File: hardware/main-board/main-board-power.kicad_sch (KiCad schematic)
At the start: 38 parts, among them J3 Power Board, J4 DMX512, U4 RT8258, U5 RT8258

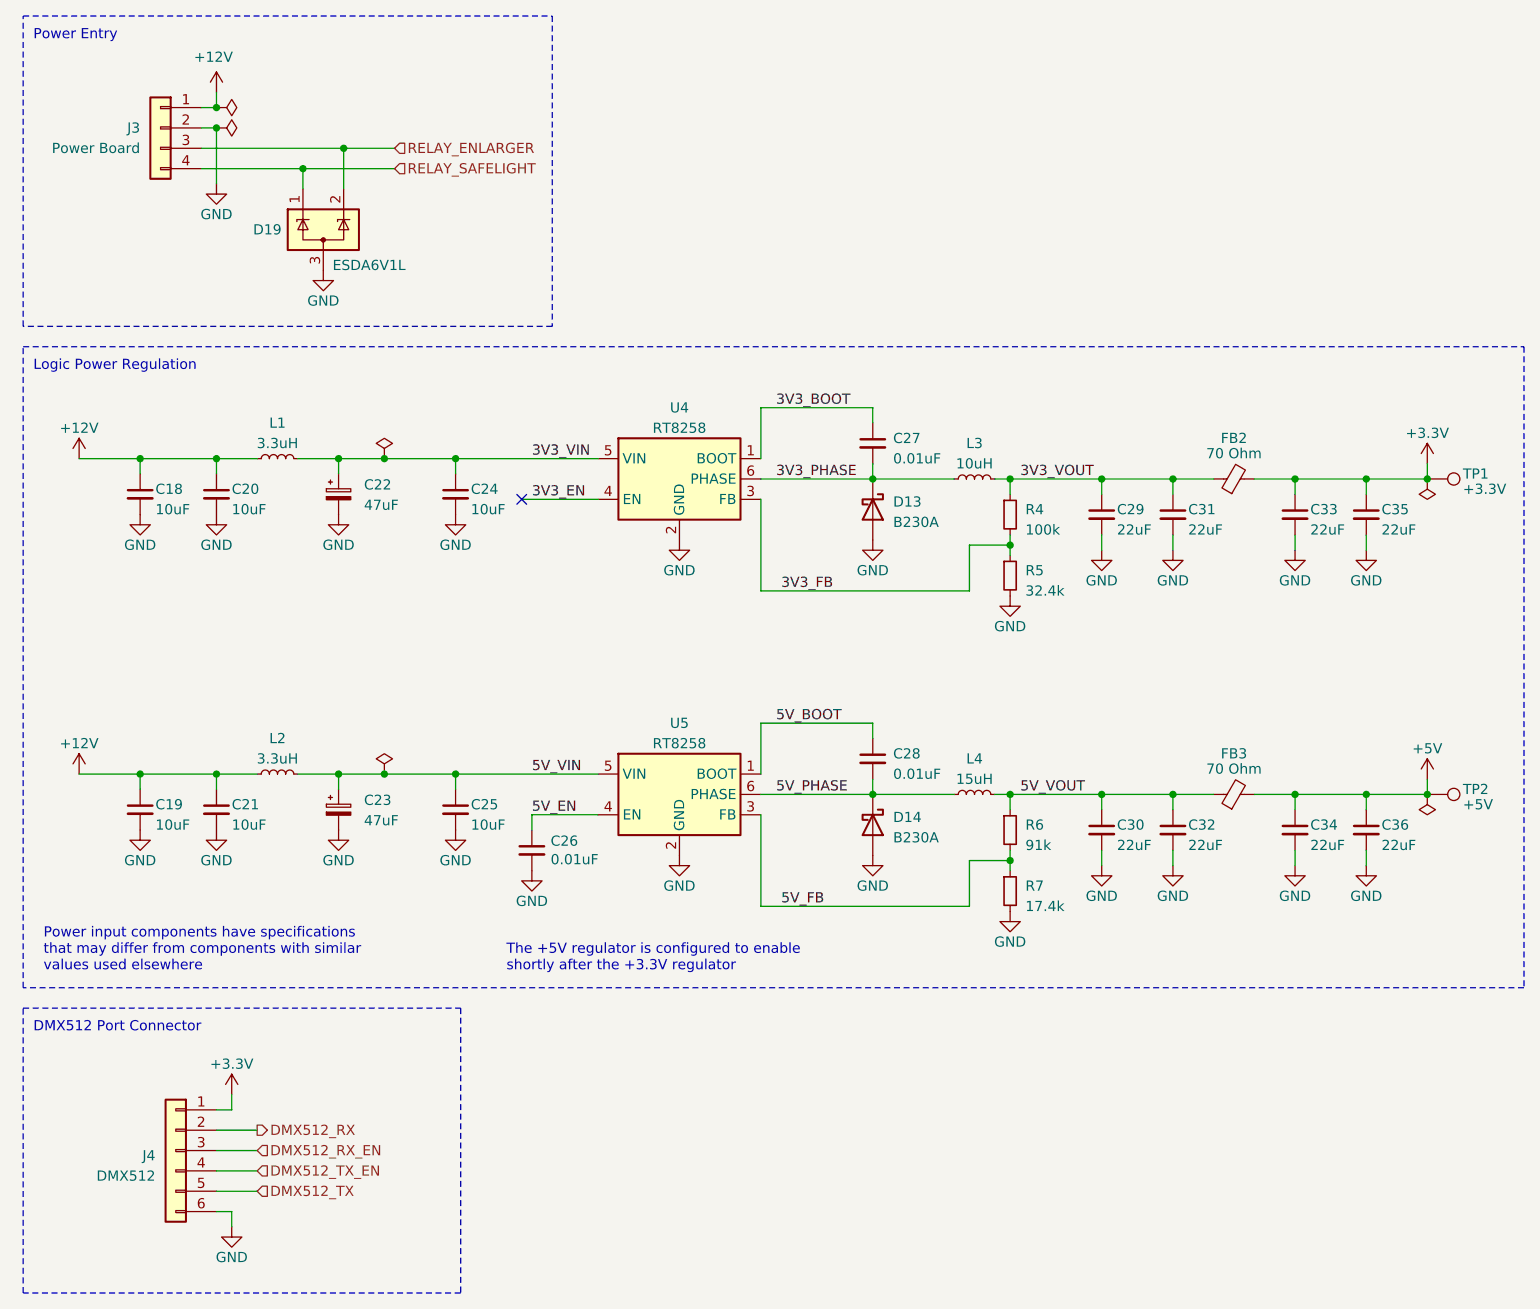
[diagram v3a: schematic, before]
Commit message: Initial replacement of main board power regulator
This is the first step towards updating the power input path for the
main board.  Right now it is mostly just a copy-paste of the TPS54294
circuit and layout from a test board, so there will be more tweaks.

Ref #67
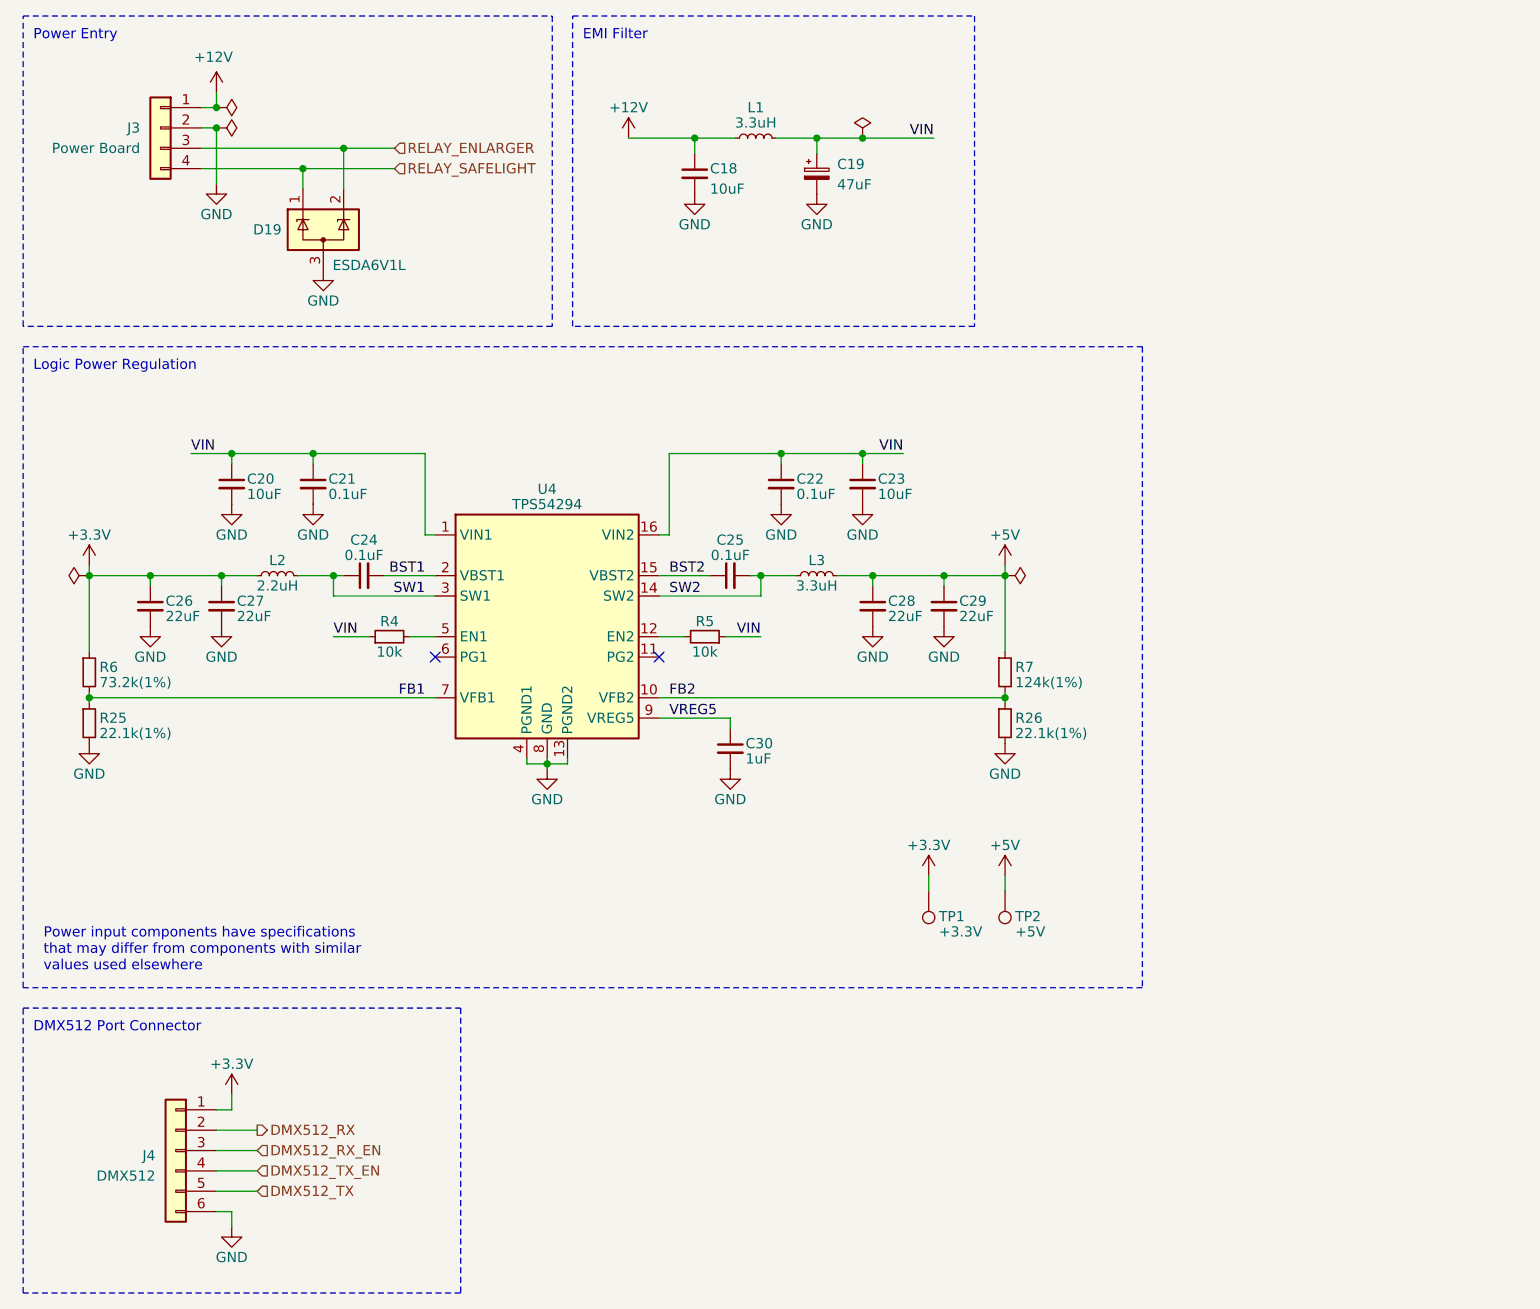
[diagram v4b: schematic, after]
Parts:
- removed C19: 10uF, Capacitor_SMD:C_1206_3216Metric, symbol Device:C_Small
- removed C22, C23: 47uF, Capacitor_SMD:CP_Elec_6.3x5.4, symbol Device:C_Polarized_Small
- removed C31, C32, C33, C34, C35, C36: 22uF, Capacitor_SMD:C_1206_3216Metric, symbol Device:C_Small
- removed D13, D14: B230A, Diode_SMD:D_SMA, symbol Diode:B230
- removed FB2, FB3: 70 Ohm, Inductor_SMD:L_0603_1608Metric, symbol Device:FerriteBead_Small
- removed L4: 15uH, Inductor_SMD:L_Taiyo-Yuden_NR-80xx, symbol Device:L_Small
- removed U4, U5: RT8258, Package_TO_SOT_SMD:TSOT-23-6, symbol Project:RT8258
- added C19: 47uF, Capacitor_SMD:CP_Elec_6.3x5.4, symbol Device:C_Polarized_Small
- added C22: 0.1uF, Capacitor_SMD:C_0603_1608Metric, symbol Device:C_Small
- added C23: 10uF, Capacitor_SMD:C_1206_3216Metric, symbol Device:C_Small
- added R25, R26: 22.1k(1%), Resistor_SMD:R_0603_1608Metric, symbol Device:R_Small
- added U4: TPS54294, lib_fp:HTSSOP-16-1EP_4.4x5mm_P0.65mm_EP3.4x5mm_Mask2.46x2.31mm_ThermalVias, symbol Project:TPS54294
- C21, C24, C25: value 10uF -> 0.1uF; footprint Capacitor_SMD:C_1206_3216Metric -> Capacitor_SMD:C_0603_1608Metric; Manufacturer PN CL31A106KAHNNNE -> CL10B104KB8NNNC; Supplier PN 1276-1075-1-ND -> 1276-1000-1-ND
- C26, C27, C28: value 0.01uF -> 22uF; footprint Capacitor_SMD:C_0603_1608Metric -> Capacitor_SMD:C_0805_2012Metric; Manufacturer PN CL10B103KB8NNNC -> CL21A226MOCLRNC; Supplier PN 1276-1009-1-ND -> 1276-6780-1-ND
- C29: footprint Capacitor_SMD:C_1206_3216Metric -> Capacitor_SMD:C_0805_2012Metric; Manufacturer PN CL31A226KAHNNNE -> CL21A226MOCLRNC; Supplier PN 1276-3047-1-ND -> 1276-6780-1-ND
- C30: value 22uF -> 1uF; footprint Capacitor_SMD:C_1206_3216Metric -> Capacitor_SMD:C_0603_1608Metric; Manufacturer PN CL31A226KAHNNNE -> CL10B105KA8NNNC; Supplier PN 1276-3047-1-ND -> 1276-1184-1-ND
- L1: footprint Inductor_SMD:L_Taiyo-Yuden_NR-50xx -> Inductor_SMD:L_TDK_VLS6045EX_VLS6045AF; Manufacturer Taiyo Yuden -> TDK Corporation; Manufacturer PN NRS5030T3R3MMGJ -> VLS6045EX-3R3N; Supplier PN 587-3459-1-ND -> 445-173052-1-ND
- L2: value 3.3uH -> 2.2uH; footprint Inductor_SMD:L_Taiyo-Yuden_NR-50xx -> Inductor_SMD:L_TDK_VLS6045EX_VLS6045AF; Manufacturer Taiyo Yuden -> TDK Corporation; Manufacturer PN NRS5030T3R3MMGJ -> VLS6045EX-2R2N; Supplier PN 587-3459-1-ND -> 445-173049-1-ND
- L3: value 10uH -> 3.3uH; footprint Inductor_SMD:L_Taiyo-Yuden_NR-80xx -> Inductor_SMD:L_TDK_VLS6045EX_VLS6045AF; Manufacturer Taiyo Yuden -> TDK Corporation; Manufacturer PN NRS8040T100MJGJ -> VLS6045EX-3R3N; Supplier PN 587-2972-1-ND -> 445-173052-1-ND
- R4: value 100k -> 10k; Manufacturer Panasonic Electronic Components -> Vishay Dale; Manufacturer PN ERJ-3EKF1003V -> CRCW060310K0JNEA; Supplier PN P100KHCT-ND -> 541-10KGCT-ND
- R5: value 32.4k -> 10k; Manufacturer Panasonic Electronic Components -> Vishay Dale; Manufacturer PN ERJ-3EKF3242V -> CRCW060310K0JNEA; Supplier PN P32.4KHCT-ND -> 541-10KGCT-ND
- R6: value 91k -> 73.2k(1%); Manufacturer Panasonic Electronic Components -> YAGEO; Manufacturer PN ERJ-3EKF9102V -> RC0603FR-0773K2L; Supplier PN P91.0KHCT-ND -> 311-73.2KHRCT-ND
- R7: value 17.4k -> 124k(1%); Manufacturer Panasonic Electronic Components -> YAGEO; Manufacturer PN ERJ-3EKF1742V -> RC0603FR-07124KL; Supplier PN P17.4KHCT-ND -> 311-124KHRCT-ND
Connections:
- net 3V3_BOOT is gone; now on net +3.3V: C27.1
- net 5V_BOOT is gone; now on net +5V: C28.1
- net 5V_EN is gone; now on net +3.3V: C26.1
- net 5V_PHASE is gone; now on net GND: C28.2
- net +12V: no longer C20.1, C21.1, L2.1
- net +3.3V: now also L2.1, R6.1
- net +5V: now also C29.1, L3.2, R7.1
- net GND: now also C27.2, C19.2, C22.2, C23.2, R25.2, R26.2, U4.13 (PGND2), U4.17 (GND), U4.4 (PGND1), U4.8 (GND); no longer C24.2, C25.2, R5.2, R7.2
- net 3V3_FB: no longer names the net of R4.2
- net 3V3_FB: now also U4.5 (EN1); no longer R5.1
- net 3V3_PHASE renamed SW2
- net SW2: now also C25.2, U4.14 (SW2); no longer C27.2
- net 3V3_VIN renamed SW1
- net SW1: now also L2.2, U4.3 (SW1); no longer L1.2
- removed net 3V3_VOUT: C29.1, L3.2, R4.1
- net 5V_FB renamed FB1
- net FB1: now also R25.1, U4.7 (VFB1); no longer R7.1
- net 5V_VIN renamed BST2
- net BST2: now also U4.15 (VBST2); no longer L2.2
- net 5V_VOUT renamed VREG5
- net VREG5: now also U4.9 (VREG5); no longer R6.1
- new net: R5.2, U4.12 (EN2)
- new net BST1: C24.2, U4.2 (VBST1)
- new net FB2: R26.1, R7.2, U4.10 (VFB2)
- new net VIN: C19.1, C20.1, C21.1, C22.1, C23.1, L1.2, R4.1, R5.1, U4.1 (VIN1), U4.16 (VIN2)
- no-connect marks 1 -> 2
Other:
- note added: "EMI Filter"
- note removed: "The +5V regulator is configured to enable shortly after the +3.3V regulator"
- moved on the sheet: TP1, TP2

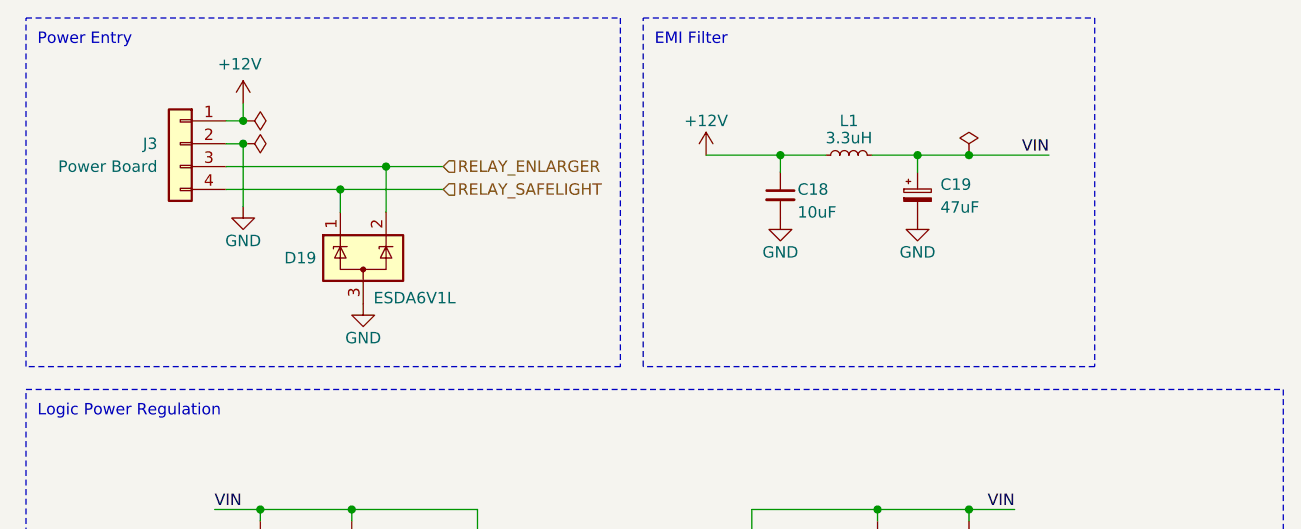
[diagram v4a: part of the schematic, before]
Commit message: Add power input filter components
For now, this is just the TVS diode and ferrite beads mentioned in the
reference app note.  For the capacitors, just using the ones from the
EMI filter as it is the next stage.

Also increased the value of the electrolytic capacitor in the EMI
filter.

Ref #67
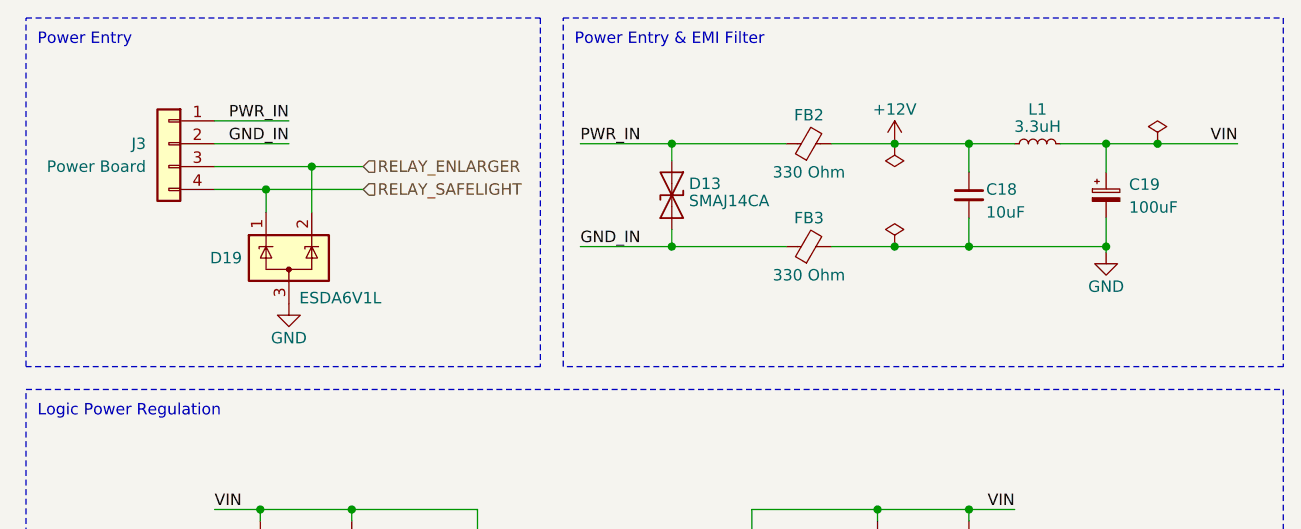
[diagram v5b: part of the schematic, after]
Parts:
- added D13: SMAJ14CA, Diode_SMD:D_SMA, symbol Diode:SMAJ14CA
- added FB2, FB3: 330 Ohm, Inductor_SMD:L_0603_1608Metric, symbol Device:FerriteBead_Small
- C19: value 47uF -> 100uF; footprint Capacitor_SMD:CP_Elec_6.3x5.4 -> lib_fp:CP_Elec_6.3x6.1; Manufacturer Kemet -> Panasonic Electronic Components; Manufacturer PN EEV476M025A9GAA -> EEE-FN1E101UP; Supplier PN 399-6717-1-ND -> 10-EEE-FN1E101UPCT-ND
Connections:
- net +12V: now also FB2.2; no longer J3.1 (Pin_1)
- net GND: now also FB3.2; no longer J3.2 (Pin_2)
- new net GND_IN: D13.2 (A2), FB3.1, J3.2 (Pin_2)
- new net PWR_IN: D13.1 (A1), FB2.1, J3.1 (Pin_1)
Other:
- note added: "Power Entry & EMI Filter"
- note removed: "EMI Filter"
- moved on the sheet: C18, C19, D19, J3, L1

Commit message: Minor BOM and silkscreen cleanup
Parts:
- C21, C22, C24, C25: Manufacturer PN CL10B104KB8NNNC -> CL10B104KA8NNNC; Supplier PN 1276-1000-1-ND -> 1276-1006-1-ND
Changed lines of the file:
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@@
 			)
 		)
-		(property "Datasheet" "https://mm.digikey.com/Volume0/opasdata/d220001/medias/docus/609/CL10B104KB8NNNC_Spec.pdf"
+		(property "Datasheet" "https://media.digikey.com/pdf/Data%20Sheets/Samsung%20PDFs/CL_Series_MLCC_ds.pdf"
 			(at 104.14 85.725 0)
 			(effects
@@
 			)
 		)
-		(property "Description" "CAP CER 0.1UF 50V X7R 0603"
+		(property "Description" "CAP CER 0.1UF 25V X7R 0603"
 			(at 104.14 85.725 0)
 			(effects
@@
 			)
 		)
-		(property "Manufacturer PN" "CL10B104KB8NNNC"
+		(property "Manufacturer PN" "CL10B104KA8NNNC"
 			(at 104.14 85.725 0)
 			(effects
@@
 			)
 		)
-		(property "Supplier PN" "1276-1000-1-ND"
+		(property "Supplier PN" "1276-1006-1-ND"
 			(at 104.14 85.725 0)
 			(effects
@@
 			)
 		)
-		(property "Datasheet" "https://mm.digikey.com/Volume0/opasdata/d220001/medias/docus/3644/CL10B105KA8NNNC_spec.pdf"
+		(property "Datasheet" "https://media.digikey.com/pdf/Data%20Sheets/Samsung%20PDFs/CL_Series_MLCC_ds.pdf"
 			(at 104.14 107.315 0)
 			(effects
@@
 			)
 		)
-		(property "Description" "CAP CER 1UF 25V X5R 0603"
+		(property "Description" "CAP CER 1UF 25V X7R 0603"
 			(at 104.14 107.315 0)
 			(effects
@@
 			)
 		)
-		(property "Datasheet" "https://mm.digikey.com/Volume0/opasdata/d220001/medias/docus/609/CL10B104KB8NNNC_Spec.pdf"
+		(property "Datasheet" "https://media.digikey.com/pdf/Data%20Sheets/Samsung%20PDFs/CL_Series_MLCC_ds.pdf"
 			(at 52.07 74.295 0)
 			(effects
@@
 			)
 		)
-		(property "Description" "CAP CER 0.1UF 50V X7R 0603"
+		(property "Description" "CAP CER 0.1UF 25V X7R 0603"
 			(at 52.07 74.295 0)
 			(effects
@@
 			)
 		)
-		(property "Manufacturer PN" "CL10B104KB8NNNC"
+		(property "Manufacturer PN" "CL10B104KA8NNNC"
 			(at 52.07 74.295 0)
 			(effects
@@
 			)
 		)
-		(property "Supplier PN" "1276-1000-1-ND"
+		(property "Supplier PN" "1276-1006-1-ND"
 			(at 52.07 74.295 0)
 			(effects
@@
 			)
 		)
-		(property "Datasheet" "https://mm.digikey.com/Volume0/opasdata/d220001/medias/docus/609/CL10B104KB8NNNC_Spec.pdf"
+		(property "Datasheet" "https://media.digikey.com/pdf/Data%20Sheets/Samsung%20PDFs/CL_Series_MLCC_ds.pdf"
 			(at 110.49 74.295 0)
 			(effects
@@
 			)
 		)
-		(property "Description" "CAP CER 0.1UF 50V X7R 0603"
+		(property "Description" "CAP CER 0.1UF 25V X7R 0603"
 			(at 110.49 74.295 0)
 			(effects
@@
 			)
 		)
-		(property "Manufacturer PN" "CL10B104KB8NNNC"
+		(property "Manufacturer PN" "CL10B104KA8NNNC"
 			(at 110.49 74.295 0)
 			(effects
@@
 			)
 		)
-		(property "Supplier PN" "1276-1000-1-ND"
+		(property "Supplier PN" "1276-1006-1-ND"
 			(at 110.49 74.295 0)
 			(effects
@@
 			)
 		)
-		(property "Datasheet" "https://mm.digikey.com/Volume0/opasdata/d220001/medias/docus/609/CL10B104KB8NNNC_Spec.pdf"
+		(property "Datasheet" "https://media.digikey.com/pdf/Data%20Sheets/Samsung%20PDFs/CL_Series_MLCC_ds.pdf"
 			(at 58.42 85.725 0)
 			(effects
@@
 			)
 		)
-		(property "Description" "CAP CER 0.1UF 50V X7R 0603"
+		(property "Description" "CAP CER 0.1UF 25V X7R 0603"
 			(at 58.42 85.725 0)
 			(effects
@@
 			)
 		)
-		(property "Manufacturer PN" "CL10B104KB8NNNC"
+		(property "Manufacturer PN" "CL10B104KA8NNNC"
 			(at 58.42 85.725 0)
 			(effects
@@
 			)
 		)
-		(property "Supplier PN" "1276-1000-1-ND"
+		(property "Supplier PN" "1276-1006-1-ND"
 			(at 58.42 85.725 0)
 			(effects
